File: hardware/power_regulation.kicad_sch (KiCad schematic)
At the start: 19 parts, among them U3 MAX6106, U4 LM27761

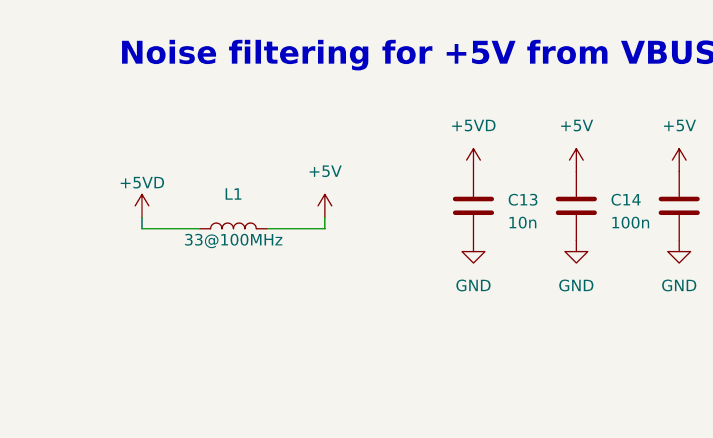
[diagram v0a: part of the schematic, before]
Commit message: wip: schematic fixes based on testing
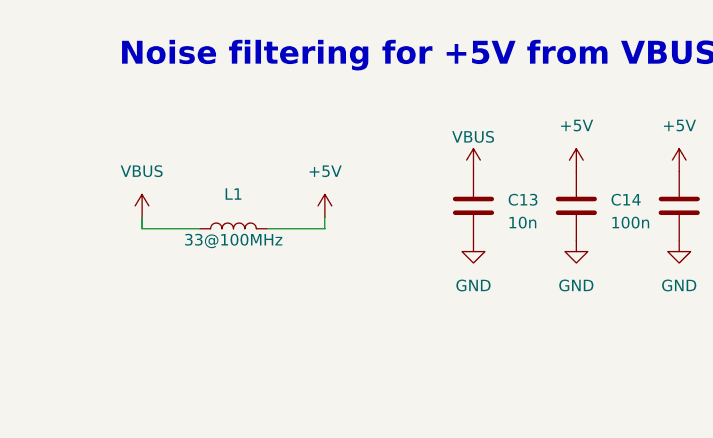
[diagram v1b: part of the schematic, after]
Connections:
- net +5VD renamed VBUS
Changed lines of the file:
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@@
   (title_block
     (title "DSP PAW add-on board")
-    (date "2023-08-19")
+    (date "2023-09-04")
+    (rev "2")
     (company "bitgloo")
     (comment 1 "Released under the CERN Open Hardware Licence Version 2 - Strongly Reciprocal")
@@
     )
   )
-  (symbol (lib_id "power:+5VD") (at 96.52 66.04 0) (unit 1)
-    (in_bom yes) (on_board yes) (dnp no)
-    (property "Reference" "#PWR017" (at 96.52 69.85 0)
-      (effects (font (size 1.27 1.27)) hide)
-    )
-    (property "Value" "+5VD" (at 96.52 60.96 0)
+  (symbol (lib_id "power:VBUS") (at 96.52 66.04 0) (unit 1)
+    (in_bom yes) (on_board yes) (dnp no) (fields_autoplaced)
+    (property "Reference" "#PWR061" (at 96.52 69.85 0)
+      (effects (font (size 1.27 1.27)) hide)
+    )
+    (property "Value" "VBUS" (at 96.52 62.23 0)
       (effects (font (size 1.27 1.27)))
     )
@@
     (instances
       (project "DSP PAW add-on board"
-        (path "/c291319b-d76e-4fda-91cc-061acff65f9f/97fc232a-dbc7-49da-a6a0-e33e9aacbabd"
-          (reference "#PWR017") (unit 1)
+        (path "/c291319b-d76e-4fda-91cc-061acff65f9f/270d19d2-3af2-41db-ad1c-33373417ec82"
+          (reference "#PWR061") (unit 1)
+        )
+        (path "/c291319b-d76e-4fda-91cc-061acff65f9f/97fc232a-dbc7-49da-a6a0-e33e9aacbabd"
+          (reference "#PWR047") (unit 1)
         )
       )
@@
         (path "/c291319b-d76e-4fda-91cc-061acff65f9f/97fc232a-dbc7-49da-a6a0-e33e9aacbabd"
           (reference "#PWR030") (unit 1)
-        )
-      )
-    )
-  )
-  (symbol (lib_id "power:+5VD") (at 59.69 71.12 0) (unit 1)
-    (in_bom yes) (on_board yes) (dnp no) (fields_autoplaced)
-    (property "Reference" "#PWR022" (at 59.69 74.93 0)
-      (effects (font (size 1.27 1.27)) hide)
-    )
-    (property "Value" "+5VD" (at 59.69 67.31 0)
-      (effects (font (size 1.27 1.27)))
-    )
-    (property "Footprint" "" (at 59.69 71.12 0)
-      (effects (font (size 1.27 1.27)) hide)
-    )
-    (property "Datasheet" "" (at 59.69 71.12 0)
-      (effects (font (size 1.27 1.27)) hide)
-    )
-    (pin "1")
-    (instances
-      (project "DSP PAW add-on board"
-        (path "/c291319b-d76e-4fda-91cc-061acff65f9f/97fc232a-dbc7-49da-a6a0-e33e9aacbabd"
-          (reference "#PWR022") (unit 1)
         )
       )
@@
         )
       )
+    )
+  )
+  (symbol (lib_id "power:VBUS") (at 59.69 71.12 0) (unit 1)
+    (in_bom yes) (on_board yes) (dnp no)
+    (property "Reference" "#PWR061" (at 59.69 74.93 0)
+      (effects (font (size 1.27 1.27)) hide)
+    )
+    (property "Value" "VBUS" (at 59.69 66.04 0)
+      (effects (font (size 1.27 1.27)))
+    )
+    (property "Footprint" "" (at 59.69 71.12 0)
+      (effects (font (size 1.27 1.27)) hide)
+    )
+    (property "Datasheet" "" (at 59.69 71.12 0)
+      (effects (font (size 1.27 1.27)) hide)
+    )
+    (pin "1")
+    (instances
+      (project "DSP PAW add-on board"
+        (path "/c291319b-d76e-4fda-91cc-061acff65f9f/270d19d2-3af2-41db-ad1c-33373417ec82"
+          (reference "#PWR061") (unit 1)
+        )
+        (path "/c291319b-d76e-4fda-91cc-061acff65f9f/97fc232a-dbc7-49da-a6a0-e33e9aacbabd"
+          (reference "#PWR051") (unit 1)
+        )
+      )

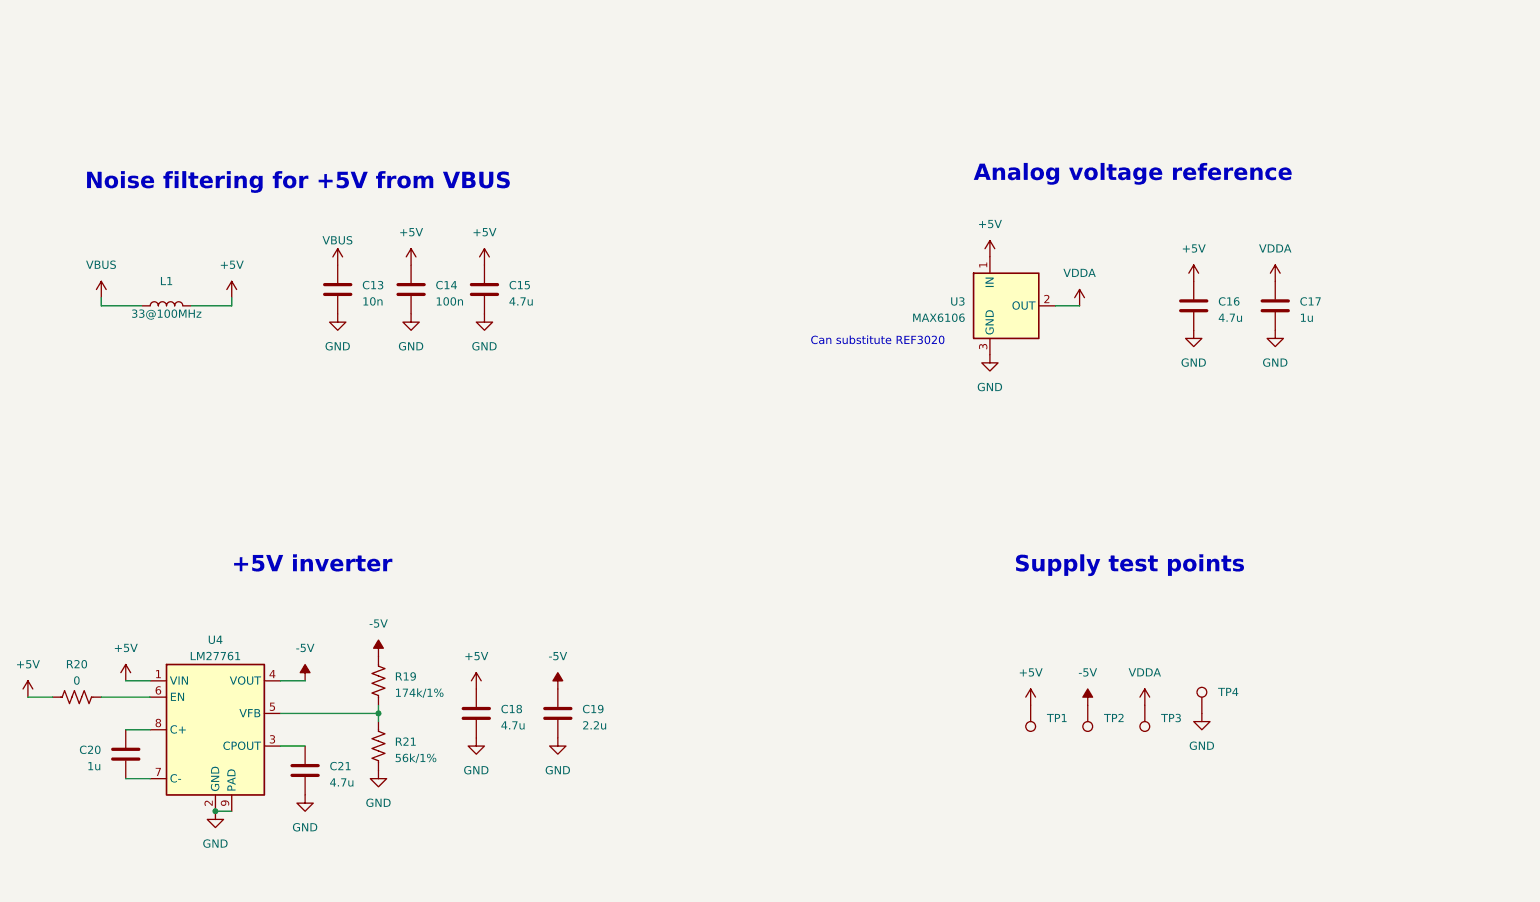
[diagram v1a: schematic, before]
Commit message: vdda buffer; vdda for pots; other fixes
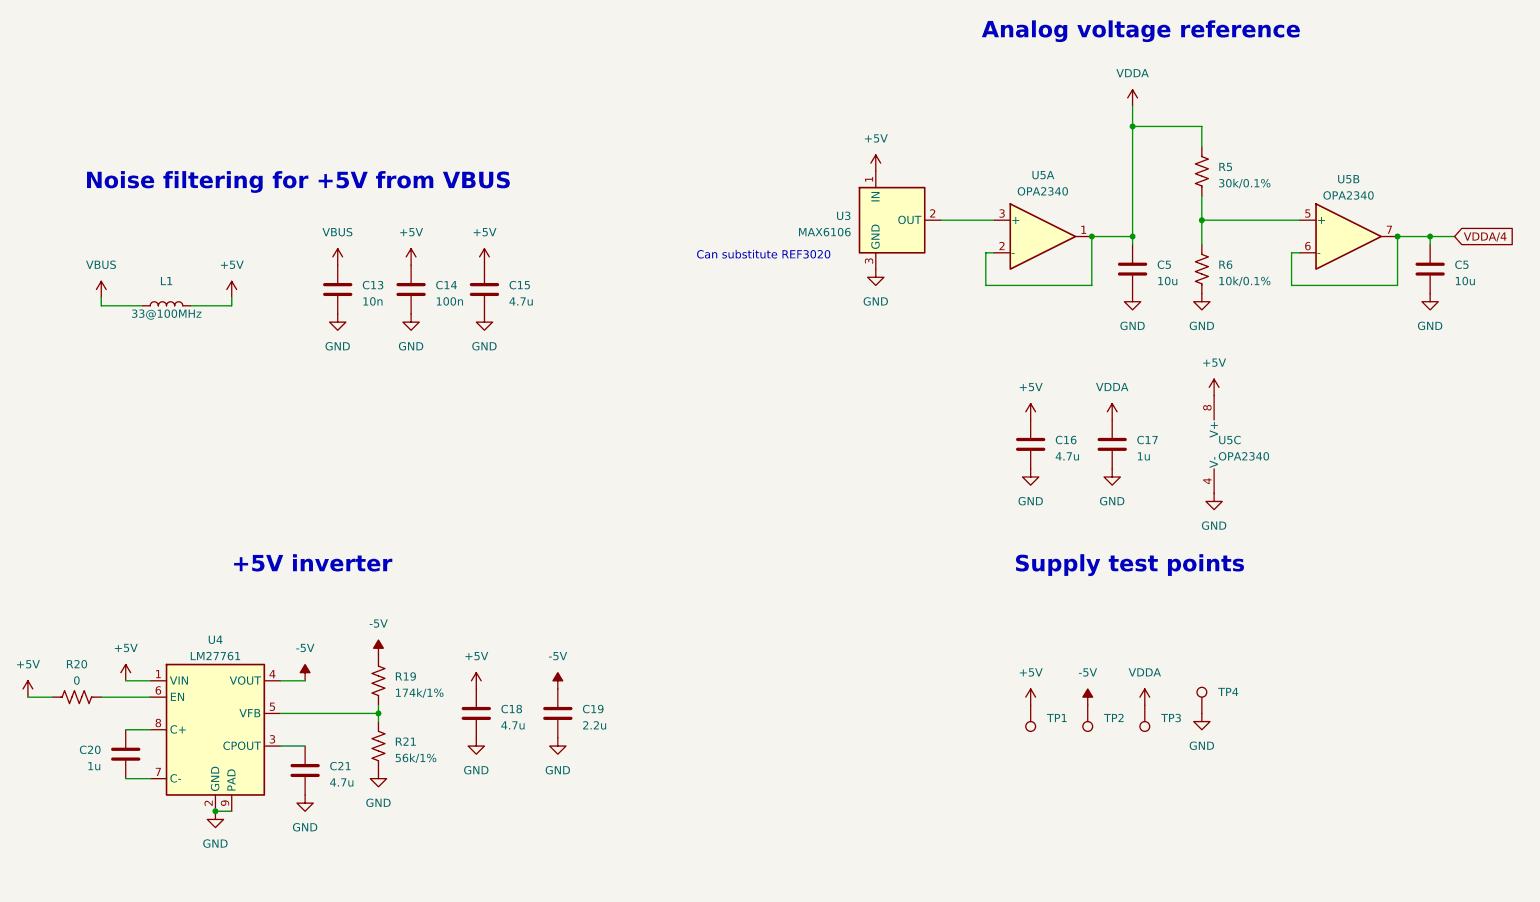
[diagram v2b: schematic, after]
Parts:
- added C5 (x2): 10u, Capacitor_SMD:C_0805_2012Metric, symbol Device:C
- added R5: 30k/0.1%, Resistor_SMD:R_0603_1608Metric, symbol Device:R_US
- added R6: 10k/0.1%, Resistor_SMD:R_0603_1608Metric, symbol Device:R_US
- added U5: OPA2340, Package_SO:TSSOP-8_3x3mm_P0.65mm, symbol Amplifier_Operational:OPA2340
- C13: LCSC Part # C57112 -> (none)
- C14: LCSC Part # C14663 -> (none)
- C15, C16, C18, C21: LCSC Part # C19666 -> (none)
- C17, C20: LCSC Part # C15849 -> (none)
- C19: LCSC Part # C23630 -> (none)
- L1: LCSC Part # C88984 -> (none)
- R19: LCSC Part # C482778 -> (none)
- R20: LCSC Part # C21189 -> (none)
- R21: LCSC Part # C5140721 -> (none)
- U3: LCSC Part # C26804 -> (none)
- U4: LCSC Part # C129351 -> (none)
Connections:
- net +5V: now also U5.8 (V+)
- net GND: now also C5.1, C5.1, R6.1, U5.4 (V-)
- net VDDA: now also C5.2, R5.2, U5.1, U5.2 (-); no longer U3.2 (OUT)
- new net: U3.2 (OUT), U5.3 (+)
- new net: R5.1, R6.2, U5.5 (+)
- new net VDDA/4: C5.2, U5.6 (-), U5.7
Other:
- moved on the sheet: C16, C17, U3

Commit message: use nucleo 3.3v vdda; add 2nd low-pass stage to input
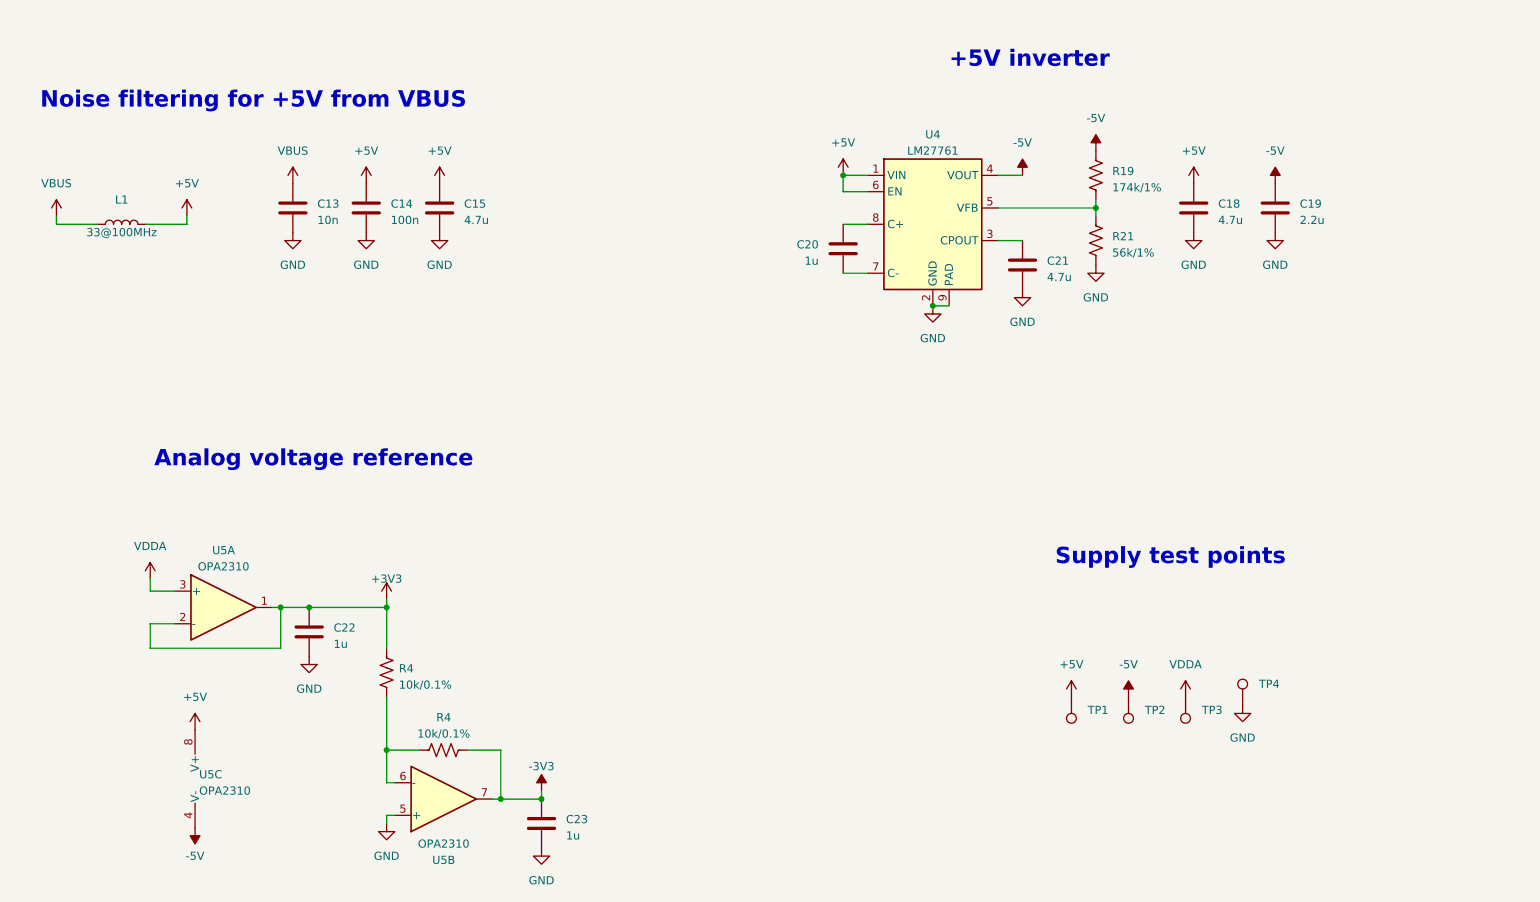
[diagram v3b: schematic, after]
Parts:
- removed C16: 4.7u, Capacitor_SMD:C_0603_1608Metric, symbol Device:C
- removed C17: 1u, Capacitor_SMD:C_0603_1608Metric, symbol Device:C
- removed C5 (x2): 10u, Capacitor_SMD:C_0805_2012Metric, symbol Device:C
- removed R20: 0, Resistor_SMD:R_0603_1608Metric, symbol Device:R_US
- removed R5: 30k/0.1%, Resistor_SMD:R_0603_1608Metric, symbol Device:R_US
- removed R6: 10k/0.1%, Resistor_SMD:R_0603_1608Metric, symbol Device:R_US
- removed U3: MAX6106, Package_TO_SOT_SMD:SOT-23, symbol Reference_Voltage:MAX6106
- added C22, C23: 1u, Capacitor_SMD:C_0603_1608Metric, symbol Device:C
- added R4 (x2): 10k/0.1%, Resistor_SMD:R_0603_1608Metric, symbol Device:R_US
- U5: value OPA2340 -> OPA2310; Part Number OPA2310IDGKR -> (none)
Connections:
- net +5V: now also U4.6 (EN)
- net -5V: now also U5.4 (V-)
- net GND: now also U5.5 (+), C22.2, C23.2; no longer U5.4 (V-)
- net VDDA: now also U5.3 (+); no longer U5.1, U5.2 (-)
- net VDDA/4: no longer names the net of U5.6 (-)
- net VDDA/4: now also R4.1, R4.1; no longer U5.7
- new net +3V3: C22.1, R4.2, U5.1, U5.2 (-)
- new net -3V3: C23.1, R4.2, U5.7
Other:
- note removed: "Can substitute REF3020"
- moved on the sheet: C13, C14, C15, C18, C19, C20, C21, L1, R19, R21, TP1, TP2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

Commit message: finalize rev2 schematic
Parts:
- R4: Part Number (none) -> RN73R1JTTD1012B25
- U5: Part Number (none) -> OPA2310IDGKR
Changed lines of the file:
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@@
       (effects (font (size 1.27 1.27)) hide)
     )
-    (property "Part Number" "" (at 104.14 129.54 0)
+    (property "Part Number" "RN73R1JTTD1012B25" (at 104.14 129.54 0)
       (effects (font (size 1.27 1.27)) hide)
     )
@@
     )
     (property "Datasheet" "" (at 76.835 146.05 0)
+      (effects (font (size 1.27 1.27)) hide)
+    )
+    (property "Part Number" "OPA2310IDGKR" (at 76.835 146.05 0)
       (effects (font (size 1.27 1.27)) hide)
     )
@@
       (effects (font (size 1.27 1.27)) hide)
     )
+    (property "Part Number" "OPA2310IDGKR" (at 113.03 149.225 0)
+      (effects (font (size 1.27 1.27)) hide)
+    )
     (pin "1")
     (pin "2")
@@
     )
     (property "Datasheet" "" (at 78.74 119.38 0)
+      (effects (font (size 1.27 1.27)) hide)
+    )
+    (property "Part Number" "OPA2310IDGKR" (at 78.74 119.38 0)
       (effects (font (size 1.27 1.27)) hide)
     )
@@
       (effects (font (size 1.27 1.27)) hide)
     )
-    (property "Part Number" "" (at 113.03 141.605 0)
-      (effects (font (size 1.27 1.27)) hide)
-    )
+    (property "Part Number" "RN73R1JTTD1012B25" (at 113.03 141.605 0)
+      (effects (font (size 1.27 1.27)) hide)
+    )

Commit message: finish rev2 layout
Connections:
- net +3V3: now also TP3.1
- net VDDA: no longer TP3.1
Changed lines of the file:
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@@
-    )
-  )
-  (symbol (lib_id "power:VDDA") (at 228.6 133.35 0) (unit 1)
-    (in_bom yes) (on_board yes) (dnp no) (fields_autoplaced)
-    (property "Reference" "#PWR013" (at 228.6 137.16 0)
-      (effects (font (size 1.27 1.27)) hide)
-    )
-    (property "Value" "VDDA" (at 228.6 128.27 0)
-      (effects (font (size 1.27 1.27)))
-    )
-    (property "Footprint" "" (at 228.6 133.35 0)
-      (effects (font (size 1.27 1.27)) hide)
-    )
-    (property "Datasheet" "" (at 228.6 133.35 0)
-      (effects (font (size 1.27 1.27)) hide)
-    )
-    (pin "1")
-    (instances
-      (project "stmdsp_rev3"
-        (path "/975c3983-57e7-4e06-a697-831e5209dd80"
-          (reference "#PWR013") (unit 1)
-        )
-      )
-      (project "DSP PAW add-on board"
-        (path "/c291319b-d76e-4fda-91cc-061acff65f9f/270d19d2-3af2-41db-ad1c-33373417ec82"
-          (reference "#PWR033") (unit 1)
-        )
-        (path "/c291319b-d76e-4fda-91cc-061acff65f9f/97fc232a-dbc7-49da-a6a0-e33e9aacbabd"
-          (reference "#PWR039") (unit 1)
-        )
-      )
     )
   )
@@
         )
       )
+    )
+  )
+  (symbol (lib_id "power:+3V3") (at 228.6 133.35 0) (unit 1)
+    (in_bom yes) (on_board yes) (dnp no)
+    (property "Reference" "#PWR04" (at 228.6 137.16 0)
+      (effects (font (size 1.27 1.27)) hide)
+    )
+    (property "Value" "+3V3" (at 227.965 128.27 0)
+      (effects (font (size 1.27 1.27)))
+    )
+    (property "Footprint" "" (at 228.6 133.35 0)
+      (effects (font (size 1.27 1.27)) hide)
+    )
+    (property "Datasheet" "" (at 228.6 133.35 0)
+      (effects (font (size 1.27 1.27)) hide)
+    )
+    (pin "1")
+    (instances
+      (project "DSP PAW add-on board"
+        (path "/c291319b-d76e-4fda-91cc-061acff65f9f/97fc232a-dbc7-49da-a6a0-e33e9aacbabd"
+          (reference "#PWR04") (unit 1)
+        )
+      )
